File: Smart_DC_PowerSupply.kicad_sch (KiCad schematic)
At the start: 4 parts, among them J1 USB_C_Receptacle_PowerOnly_24P, U0 TPS259620DDAR, U1 ADP150AUJZ-3.3-R7, U5_1 ADP7105ARDZ-3.3-R7

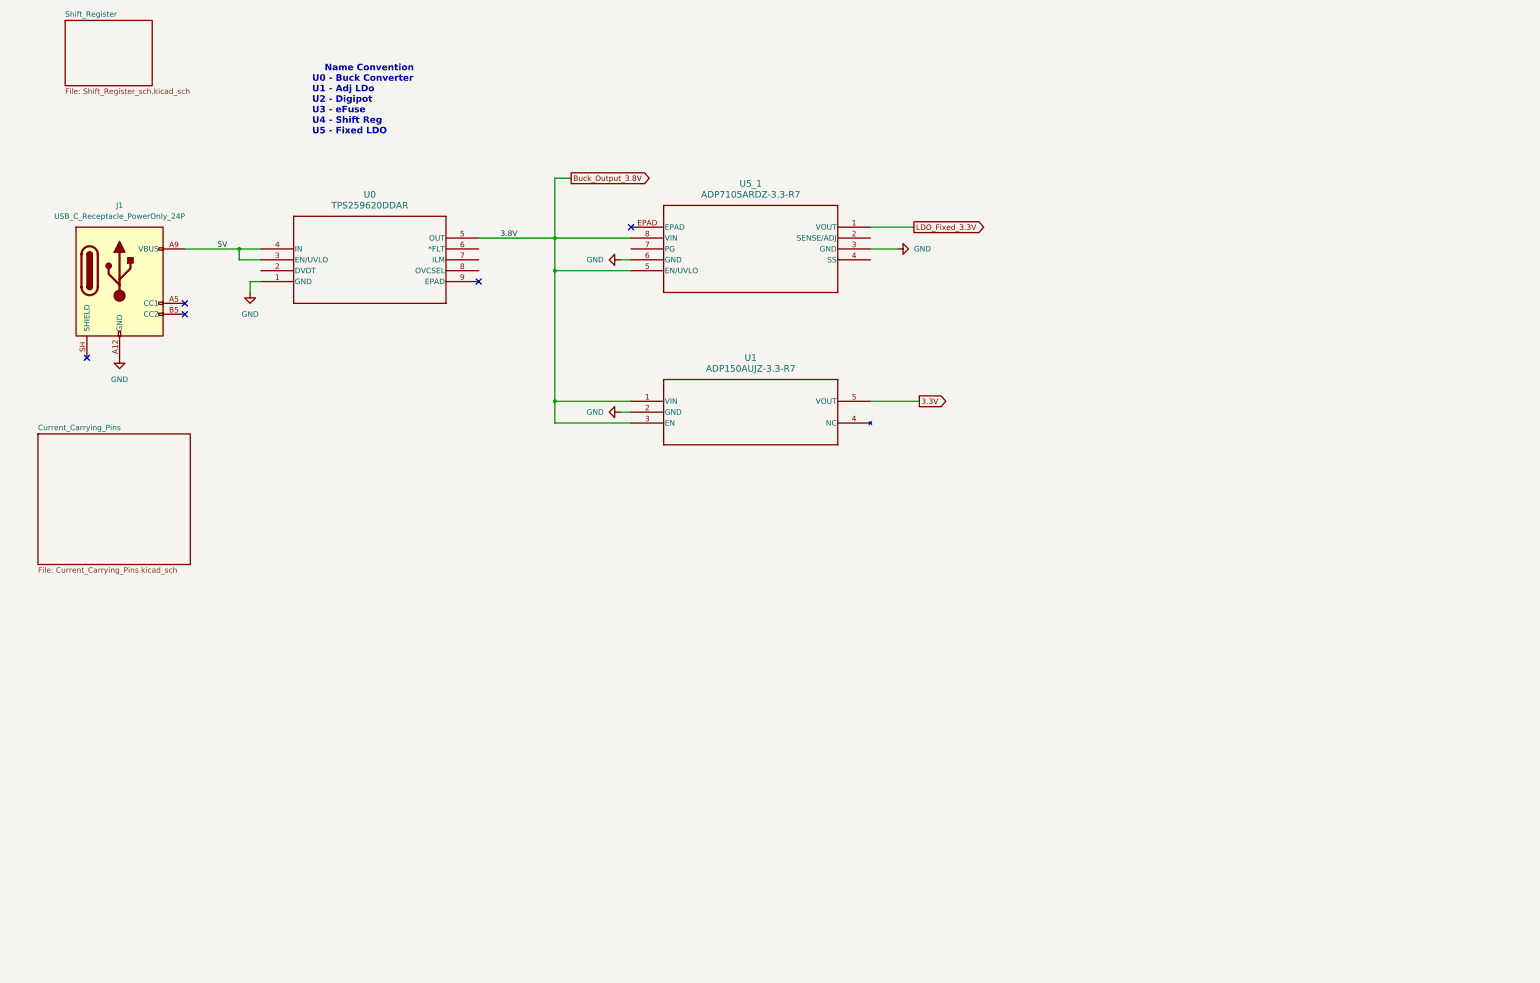
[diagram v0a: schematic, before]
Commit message: Full schematic connection without ratio consideration.
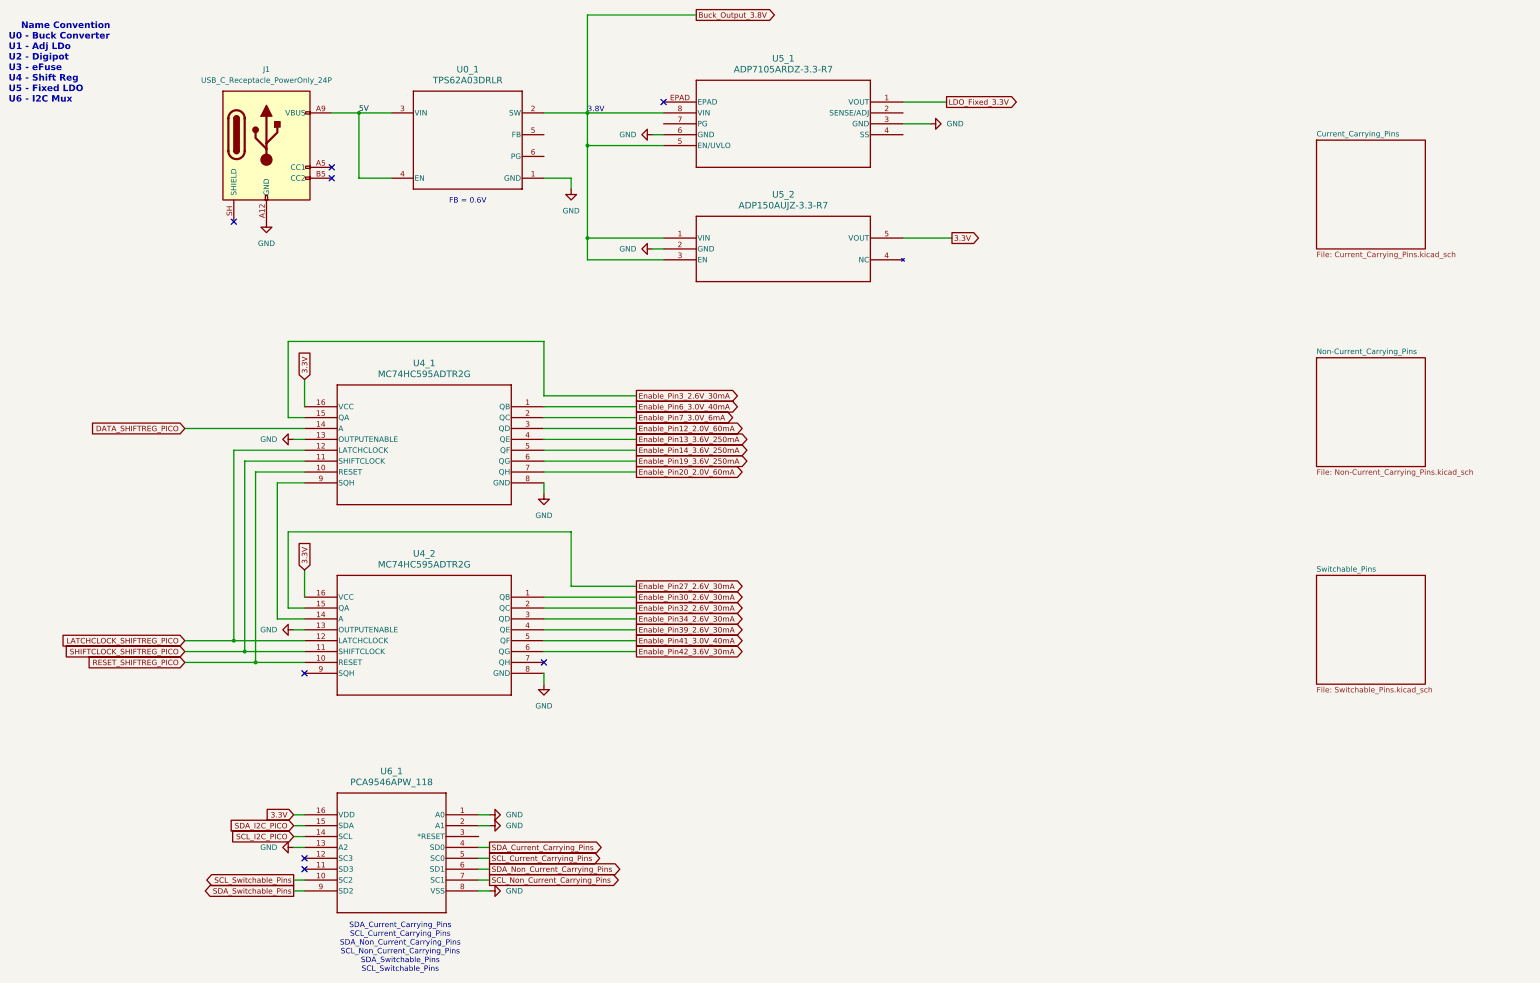
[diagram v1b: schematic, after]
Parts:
- removed U0: TPS259620DDAR, SOIC_20DDAR_TEX, symbol eFuse for electronic:TPS259620DDAR
- added U0_1: TPS62A03DRLR, DRL0006A-MFG, symbol Buck Converter:TPS62A03DRLR
- added U4_1, U4_2: MC74HC595ADTR2G, TSSOP-16_ONS, symbol Tiny 8-bit shift register:MC74HC595ADTR2G
- added U6_1: PCA9546APW_118, TSSOP16_SOT403-1_NXP, symbol I2C 4-channel Multiplexor:PCA9546APW_118
- renumbered U1 to U5_2
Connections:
- net 3.3V: now also U4_1.16 (VCC), U4_2.16 (VCC), U6_1.16 (VDD)
- net 5V: now also U0_1.3 (VIN), U0_1.4 (EN)
- net Buck_Output_3.8V: now also U0_1.2 (SW)
- net GND: now also U0_1.1 (GND), U4_1.13 (OUTPUTENABLE), U4_1.8 (GND), U4_2.13 (OUTPUTENABLE), U4_2.8 (GND), U6_1.1 (A0), U6_1.13 (A2), U6_1.2 (A1), U6_1.8 (VSS)
- new net: U4_1.9 (SQH), U4_2.14 (A)
- new net DATA_SHIFTREG_PICO: U4_1.14 (A)
- new net Enable_Pin12_2.0V_60mA: U4_1.3 (QD)
- new net Enable_Pin13_3.6V_250mA: U4_1.4 (QE)
- new net Enable_Pin14_3.6V_250mA: U4_1.5 (QF)
- new net Enable_Pin19_3.6V_250mA: U4_1.6 (QG)
- new net Enable_Pin20_2.0V_60mA: U4_1.7 (QH)
- new net Enable_Pin27_2.6V_30mA: U4_2.15 (QA)
- new net Enable_Pin30_2.6V_30mA: U4_2.1 (QB)
- new net Enable_Pin32_2.6V_30mA: U4_2.2 (QC)
- new net Enable_Pin34_2.6V_30mA: U4_2.3 (QD)
- new net Enable_Pin39_2.6V_30mA: U4_2.4 (QE)
- new net Enable_Pin3_2.6V_30mA: U4_1.15 (QA)
- new net Enable_Pin41_3.0V_40mA: U4_2.5 (QF)
- new net Enable_Pin42_3.6V_30mA: U4_2.6 (QG)
- new net Enable_Pin6_3.0V_40mA: U4_1.1 (QB)
- new net Enable_Pin7_3.0V_6mA: U4_1.2 (QC)
- new net LATCHCLOCK_SHIFTREG_PICO: U4_1.12 (LATCHCLOCK), U4_2.12 (LATCHCLOCK)
- new net RESET_SHIFTREG_PICO: U4_1.10 (RESET), U4_2.10 (RESET)
- new net SCL_Current_Carrying_Pins: U6_1.5 (SC0)
- new net SCL_I2C_PICO: U6_1.14 (SCL)
- new net SCL_Non_Current_Carrying_Pins: U6_1.7 (SC1)
- new net SCL_Switchable_Pins: U6_1.10 (SC2)
- new net SDA_Current_Carrying_Pins: U6_1.4 (SD0)
- new net SDA_I2C_PICO: U6_1.15 (SDA)
- new net SDA_Non_Current_Carrying_Pins: U6_1.6 (SD1)
- new net SDA_Switchable_Pins: U6_1.9 (SD2)
- new net SHIFTCLOCK_SHIFTREG_PICO: U4_1.11 (SHIFTCLOCK), U4_2.11 (SHIFTCLOCK)
- no-connect marks 5 -> 8
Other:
- removed sheet Shift_Register
- added sheet Non-Current_Carrying_Pins (Non-Current_Carrying_Pins.kicad_sch)
- added sheet Switchable_Pins (Switchable_Pins.kicad_sch)
- note added: "3.8V"
- note added: "FB = 0.6V"
- note added: "Name Convention U0 - Buck Converter U1 - Adj LDo U2 - Digipot U3 - eFuse U4 - Shift Reg U5 - Fixed LDO U6 - I2C Mux"
- note added: "SDA_Current_Carrying_Pins SCL_Current_Carrying_Pins SDA_Non_Current_Carrying_Pins SCL_Non_Current_Carrying_Pins SDA_Switchable_Pins SCL_Switchable_Pins"
- note removed: "Name Convention U0 - Buck Converter U1 - Adj LDo U2 - Digipot U3 - eFuse U4 - Shift Reg U5 - Fixed LDO"
- moved on the sheet: J1, U5_1, U5_2
